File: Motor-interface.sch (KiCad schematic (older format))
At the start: 0 parts

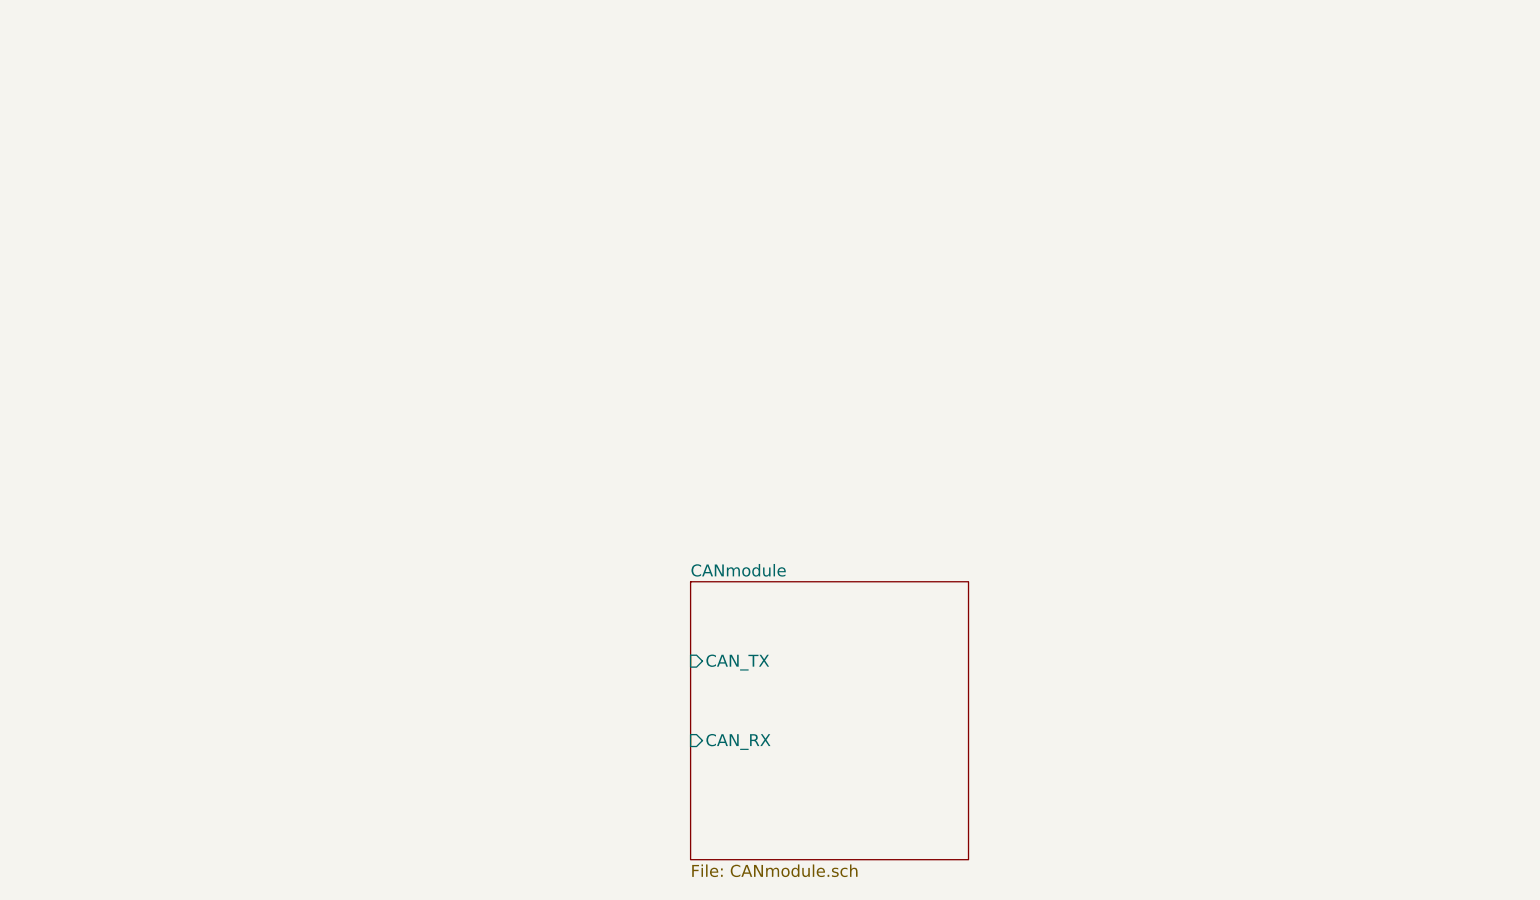
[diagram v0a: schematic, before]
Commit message: added digital pot
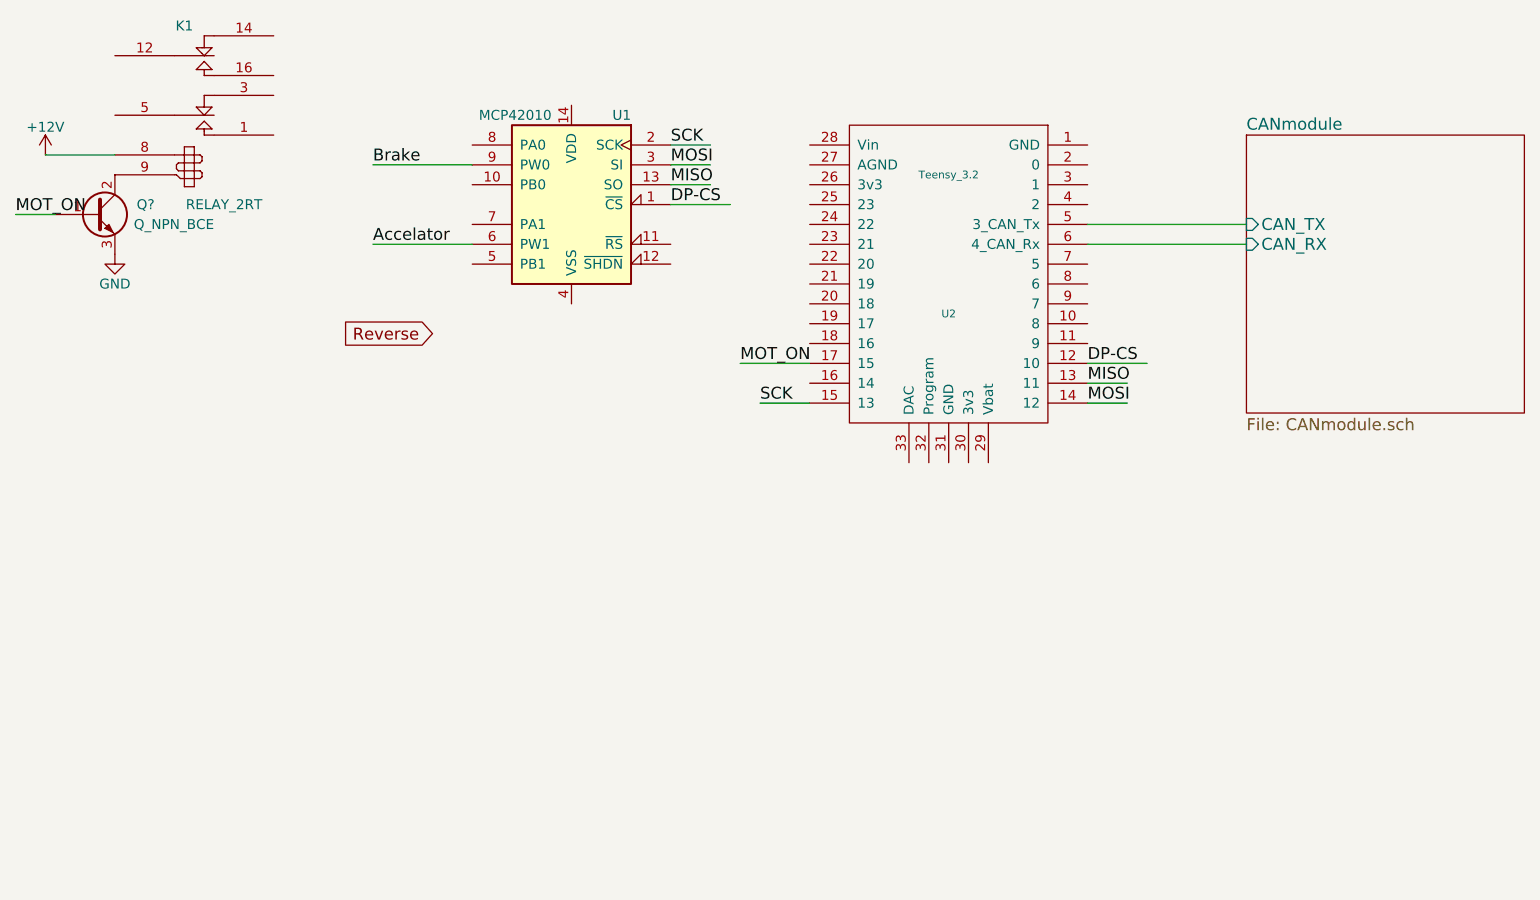
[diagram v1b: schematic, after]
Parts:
- added K1: RELAY_2RT, symbol RELAY_2RT
- added Q?: Q_NPN_BCE, symbol Q_NPN_BCE
- added U1: MCP42010, symbol MCP42010
- added U2: Teensy_3.2, symbol Teensy_3.2
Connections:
- net labels added: +12V, Accelator, Brake, DP-CS, GND, MISO, MOSI, MOT_ON, Reverse, SCK
- wire segments 0 -> 15
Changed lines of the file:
@@
 $EndDescr
 $Sheet
-S 4000 4350 1400 1400
+S 6800 2100 1400 1400
 U 57FCAC7A
 F0 "CANmodule" 60
 F1 "CANmodule.sch" 60
-F2 "CAN_TX" I L 4000 4750 60
-F3 "CAN_RX" I L 4000 5150 60
+F2 "CAN_TX" I L 6800 2550 60
+F3 "CAN_RX" I L 6800 2650 60
 $EndSheet
+$Comp
+L Teensy_3.2 U2
+U 1 1 57FC913B
+P 5300 2850
+F 0 "U2" H 5300 2700 39  0000 C CNN
+F 1 "Teensy_3.2" H 5300 3400 39  0000 C CNN
+F 2 "" H 5000 2400 39  0000 C CNN
+F 3 "" H 5000 2400 39  0000 C CNN
+	1    5300 2850
+	-1   0    0    -1
+$EndComp
+$Comp
+L MCP42010 U1
+U 1 1 57FC991B
+P 3400 2450
+F 0 "U1" H 3100 2900 50  0000 L CNN
+F 1 "MCP42010" H 3500 2900 50  0000 L CNN
+F 2 "" H 3400 2550 50  0000 C CNN
+F 3 "" H 3400 2550 50  0000 C CNN
+	1    3400 2450
+	-1   0    0    -1
+$EndComp
+Wire Wire Line
+	2900 2250 2400 2250
+Text Label 2400 2650 0    60   ~ 0
+Accelator
+Text Label 2400 2250 0    60   ~ 0
+Brake
+Text GLabel 2700 3100 0    60   Input ~ 0
+Reverse
+Wire Wire Line
+	2900 2650 2400 2650
+Text Label 3900 2150 0    60   ~ 0
+SCK
+Wire Wire Line
+	6800 2550 6000 2550
+Wire Wire Line
+	6000 2650 6800 2650
+Text Label 4350 3450 0    60   ~ 0
+SCK
+Wire Wire Line
+	4350 3450 4600 3450
+Wire Wire Line
+	3900 2150 4100 2150
+Text Label 3900 2450 0    60   ~ 0
+DP-CS
+Text Label 6000 3250 0    60   ~ 0
+DP-CS
+Wire Wire Line
+	6000 3250 6300 3250
+Wire Wire Line
+	3900 2450 4200 2450
+Text Label 3900 2350 0    60   ~ 0
+MISO
+Text Label 3900 2250 0    60   ~ 0
+MOSI
+Wire Wire Line
+	3900 2250 4100 2250
+Wire Wire Line
+	3900 2350 4100 2350
+Text Label 6000 3350 0    60   ~ 0
+MISO
+Text Label 6000 3450 0    60   ~ 0
+MOSI
+Wire Wire Line
+	6000 3350 6200 3350
+Wire Wire Line
+	6000 3450 6200 3450
+$Comp
+L RELAY_2RT K1
+U 1 1 57FCBA72
+P 1500 1950
+F 0 "K1" H 1450 2350 50  0000 C CNN
+F 1 "RELAY_2RT" H 1650 1450 50  0000 C CNN
+F 2 "" H 1500 1950 50  0000 C CNN
+F 3 "" H 1500 1950 50  0000 C CNN
+	1    1500 1950
+	1    0    0    -1
+$EndComp
+$Comp
+L Q_NPN_BCE Q?
+U 1 1 57FCBE60
+P 1000 2500
+F 0 "Q?" H 1300 2550 50  0000 R CNN
+F 1 "Q_NPN_BCE" H 1600 2450 50  0000 R CNN
+F 2 "" H 1200 2600 50  0000 C CNN
+F 3 "" H 1000 2500 50  0000 C CNN
+	1    1000 2500
+	1    0    0    -1
+$EndComp
+Wire Wire Line
+	750  2200 1100 2200
+$Comp
+L +12V #PWR?
+U 1 1 57FCC08A
+P 750 2200
+F 0 "#PWR?" H 750 2050 50  0001 C CNN
+F 1 "+12V" H 750 2340 50  0000 C CNN
+F 2 "" H 750 2200 50  0000 C CNN
+F 3 "" H 750 2200 50  0000 C CNN
+	1    750  2200
+	-1   0    0    -1
+$EndComp
+$Comp
+L GND #PWR?
+U 1 1 57FCC1C9
+P 1100 2700
+F 0 "#PWR?" H 1100 2450 50  0001 C CNN
+F 1 "GND" H 1100 2550 50  0000 C CNN
+F 2 "" H 1100 2700 50  0000 C CNN
+F 3 "" H 1100 2700 50  0000 C CNN
+	1    1100 2700
+	1    0    0    -1
+$EndComp
+Text Label 600  2500 0    60   ~ 0
+MOT_ON
+Wire Wire Line
+	600  2500 800  2500
+Text Label 4250 3250 0    60   ~ 0
+MOT_ON
+Wire Wire Line
+	4250 3250 4600 3250
 $EndSCHEMATC

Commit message: edited wiring
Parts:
- added P?: CONN_01X02, symbol CONN_01X02
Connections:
- net labels added: +3.3V
- wire segments 15 -> 22
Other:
- moved on the sheet: K1, Q?, U1, U2
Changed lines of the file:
@@
 $EndDescr
 $Sheet
-S 6800 2100 1400 1400
+S 8550 2100 1400 1400
 U 57FCAC7A
 F0 "CANmodule" 60
 F1 "CANmodule.sch" 60
-F2 "CAN_TX" I L 6800 2550 60
-F3 "CAN_RX" I L 6800 2650 60
+F2 "CAN_TX" I L 8550 2550 60
+F3 "CAN_RX" I L 8550 2650 60
 $EndSheet
 $Comp
 L Teensy_3.2 U2
 U 1 1 57FC913B
-P 5300 2850
-F 0 "U2" H 5300 2700 39  0000 C CNN
-F 1 "Teensy_3.2" H 5300 3400 39  0000 C CNN
-F 2 "" H 5000 2400 39  0000 C CNN
-F 3 "" H 5000 2400 39  0000 C CNN
-	1    5300 2850
+P 7050 2850
+F 0 "U2" H 7050 2700 39  0000 C CNN
+F 1 "Teensy_3.2" H 7050 3400 39  0000 C CNN
+F 2 "" H 6750 2400 39  0000 C CNN
+F 3 "" H 6750 2400 39  0000 C CNN
+	1    7050 2850
 	-1   0    0    -1
 $EndComp
@@
 L MCP42010 U1
 U 1 1 57FC991B
-P 3400 2450
-F 0 "U1" H 3100 2900 50  0000 L CNN
-F 1 "MCP42010" H 3500 2900 50  0000 L CNN
-F 2 "" H 3400 2550 50  0000 C CNN
-F 3 "" H 3400 2550 50  0000 C CNN
-	1    3400 2450
-	-1   0    0    -1
-$EndComp
-Wire Wire Line
-	2900 2250 2400 2250
-Text Label 2400 2650 0    60   ~ 0
+P 5150 2450
+F 0 "U1" H 4850 2900 50  0000 L CNN
+F 1 "MCP42010" H 5250 2900 50  0000 L CNN
+F 2 "" H 5150 2550 50  0000 C CNN
+F 3 "" H 5150 2550 50  0000 C CNN
+	1    5150 2450
+	-1   0    0    -1
+$EndComp
+Wire Wire Line
+	4650 2250 4150 2250
+Text Label 4150 2650 0    60   ~ 0
 Accelator
-Text Label 2400 2250 0    60   ~ 0
+Text Label 4150 2250 0    60   ~ 0
 Brake
-Text GLabel 2700 3100 0    60   Input ~ 0
+Text GLabel 4450 3100 0    60   Input ~ 0
 Reverse
 Wire Wire Line
-	2900 2650 2400 2650
-Text Label 3900 2150 0    60   ~ 0
+	4650 2650 4150 2650
+Text Label 5650 2150 0    60   ~ 0
 SCK
 Wire Wire Line
-	6800 2550 6000 2550
-Wire Wire Line
-	6000 2650 6800 2650
-Text Label 4350 3450 0    60   ~ 0
+	8550 2550 7750 2550
+Wire Wire Line
+	7750 2650 8550 2650
+Text Label 6100 3450 0    60   ~ 0
 SCK
 Wire Wire Line
-	4350 3450 4600 3450
-Wire Wire Line
-	3900 2150 4100 2150
-Text Label 3900 2450 0    60   ~ 0
+	6100 3450 6350 3450
+Wire Wire Line
+	5650 2150 5850 2150
+Text Label 5650 2450 0    60   ~ 0
 DP-CS
-Text Label 6000 3250 0    60   ~ 0
+Text Label 7750 3250 0    60   ~ 0
 DP-CS
 Wire Wire Line
-	6000 3250 6300 3250
-Wire Wire Line
-	3900 2450 4200 2450
-Text Label 3900 2350 0    60   ~ 0
+	7750 3250 8050 3250
+Wire Wire Line
+	5650 2450 5950 2450
+Text Label 5650 2350 0    60   ~ 0
 MISO
-Text Label 3900 2250 0    60   ~ 0
+Text Label 5650 2250 0    60   ~ 0
 MOSI
 Wire Wire Line
-	3900 2250 4100 2250
-Wire Wire Line
-	3900 2350 4100 2350
-Text Label 6000 3350 0    60   ~ 0
+	5650 2250 5850 2250
+Wire Wire Line
+	5650 2350 5850 2350
+Text Label 7750 3350 0    60   ~ 0
 MISO
-Text Label 6000 3450 0    60   ~ 0
+Text Label 7750 3450 0    60   ~ 0
 MOSI
 Wire Wire Line
-	6000 3350 6200 3350
-Wire Wire Line
-	6000 3450 6200 3450
+	7750 3350 7950 3350
+Wire Wire Line
+	7750 3450 7950 3450
 $Comp
 L RELAY_2RT K1
 U 1 1 57FCBA72
-P 1500 1950
-F 0 "K1" H 1450 2350 50  0000 C CNN
-F 1 "RELAY_2RT" H 1650 1450 50  0000 C CNN
-F 2 "" H 1500 1950 50  0000 C CNN
-F 3 "" H 1500 1950 50  0000 C CNN
-	1    1500 1950
+P 1900 2200
+F 0 "K1" H 1850 2600 50  0000 C CNN
+F 1 "RELAY_2RT" H 2050 1700 50  0000 C CNN
+F 2 "" H 1900 2200 50  0000 C CNN
+F 3 "" H 1900 2200 50  0000 C CNN
+	1    1900 2200
 	1    0    0    -1
 $EndComp
@@
 L Q_NPN_BCE Q?
 U 1 1 57FCBE60
-P 1000 2500
-F 0 "Q?" H 1300 2550 50  0000 R CNN
-F 1 "Q_NPN_BCE" H 1600 2450 50  0000 R CNN
-F 2 "" H 1200 2600 50  0000 C CNN
-F 3 "" H 1000 2500 50  0000 C CNN
-	1    1000 2500
-	1    0    0    -1
-$EndComp
-Wire Wire Line
-	750  2200 1100 2200
+P 1400 2750
+F 0 "Q?" H 1700 2800 50  0000 R CNN
+F 1 "Q_NPN_BCE" H 2000 2700 50  0000 R CNN
+F 2 "" H 1600 2850 50  0000 C CNN
+F 3 "" H 1400 2750 50  0000 C CNN
+	1    1400 2750
+	1    0    0    -1
+$EndComp
+Wire Wire Line
+	1150 2450 1500 2450
 $Comp
 L +12V #PWR?
 U 1 1 57FCC08A
-P 750 2200
-F 0 "#PWR?" H 750 2050 50  0001 C CNN
-F 1 "+12V" H 750 2340 50  0000 C CNN
-F 2 "" H 750 2200 50  0000 C CNN
-F 3 "" H 750 2200 50  0000 C CNN
-	1    750  2200
+P 1150 2450
+F 0 "#PWR?" H 1150 2300 50  0001 C CNN
+F 1 "+12V" H 1150 2590 50  0000 C CNN
+F 2 "" H 1150 2450 50  0000 C CNN
+F 3 "" H 1150 2450 50  0000 C CNN
+	1    1150 2450
 	-1   0    0    -1
 $EndComp
@@
 L GND #PWR?
 U 1 1 57FCC1C9
-P 1100 2700
-F 0 "#PWR?" H 1100 2450 50  0001 C CNN
-F 1 "GND" H 1100 2550 50  0000 C CNN
-F 2 "" H 1100 2700 50  0000 C CNN
-F 3 "" H 1100 2700 50  0000 C CNN
-	1    1100 2700
-	1    0    0    -1
-$EndComp
-Text Label 600  2500 0    60   ~ 0
+P 1500 2950
+F 0 "#PWR?" H 1500 2700 50  0001 C CNN
+F 1 "GND" H 1500 2800 50  0000 C CNN
+F 2 "" H 1500 2950 50  0000 C CNN
+F 3 "" H 1500 2950 50  0000 C CNN
+	1    1500 2950
+	1    0    0    -1
+$EndComp
+Text Label 1000 2750 0    60   ~ 0
 MOT_ON
 Wire Wire Line
-	600  2500 800  2500
-Text Label 4250 3250 0    60   ~ 0
+	1000 2750 1200 2750
+Text Label 6000 3250 0    60   ~ 0
 MOT_ON
 Wire Wire Line
-	4250 3250 4600 3250
+	6000 3250 6350 3250
+$Comp
+L +3.3V #PWR?
+U 1 1 58059323
+P 3850 2150
+F 0 "#PWR?" H 3850 2000 50  0001 C CNN
+F 1 "+3.3V" H 3850 2290 50  0000 C CNN
+F 2 "" H 3850 2150 50  0000 C CNN
+F 3 "" H 3850 2150 50  0000 C CNN
+	1    3850 2150
+	1    0    0    -1
+$EndComp
+$Comp
+L +3.3V #PWR?
+U 1 1 5805934B
+P 3850 2550
+F 0 "#PWR?" H 3850 2400 50  0001 C CNN
+F 1 "+3.3V" H 3850 2690 50  0000 C CNN
+F 2 "" H 3850 2550 50  0000 C CNN
+F 3 "" H 3850 2550 50  0000 C CNN
+	1    3850 2550
+	-1   0    0    -1
+$EndComp
+Wire Wire Line
+	3850 2150 4650 2150
+Wire Wire Line
+	3850 2550 4650 2550
+$Comp
+L CONN_01X02 P?
+U 1 1 5805A054
+P 1550 950
+F 0 "P?" H 1550 1100 50  0000 C CNN
+F 1 "CONN_01X02" V 1650 950 50  0000 C CNN
+F 2 "" H 1550 950 50  0000 C CNN
+F 3 "" H 1550 950 50  0000 C CNN
+	1    1550 950
+	0    1    -1   0
+$EndComp
+Wire Wire Line
+	850  1450 850  1350
+Wire Wire Line
+	1500 1150 1500 1950
+Wire Wire Line
+	1600 1150 2450 1150
+Wire Wire Line
+	2450 1150 2450 2050
+Wire Wire Line
+	2450 2050 2300 2050
+$Comp
+L GND #PWR?
+U 1 1 5805B577
+P 4650 2350
+F 0 "#PWR?" H 4650 2100 50  0001 C CNN
+F 1 "GND" H 4650 2200 50  0000 C CNN
+F 2 "" H 4650 2350 50  0000 C CNN
+F 3 "" H 4650 2350 50  0000 C CNN
+	1    4650 2350
+	1    0    0    -1
+$EndComp
+$Comp
+L GND #PWR?
+U 1 1 5805B5A1
+P 4650 2750
+F 0 "#PWR?" H 4650 2500 50  0001 C CNN
+F 1 "GND" H 4650 2600 50  0000 C CNN
+F 2 "" H 4650 2750 50  0000 C CNN
+F 3 "" H 4650 2750 50  0000 C CNN
+	1    4650 2750
+	1    0    0    -1
+$EndComp
 $EndSCHEMATC
